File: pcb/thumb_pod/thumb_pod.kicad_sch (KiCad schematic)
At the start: 17 parts, among them J1 Conn_02x06_Odd_Even, SW1 SW_Push, SW2 SW_Push, SW3 SW_Push, SW4 SW_Push, U1 RKJXM1015004

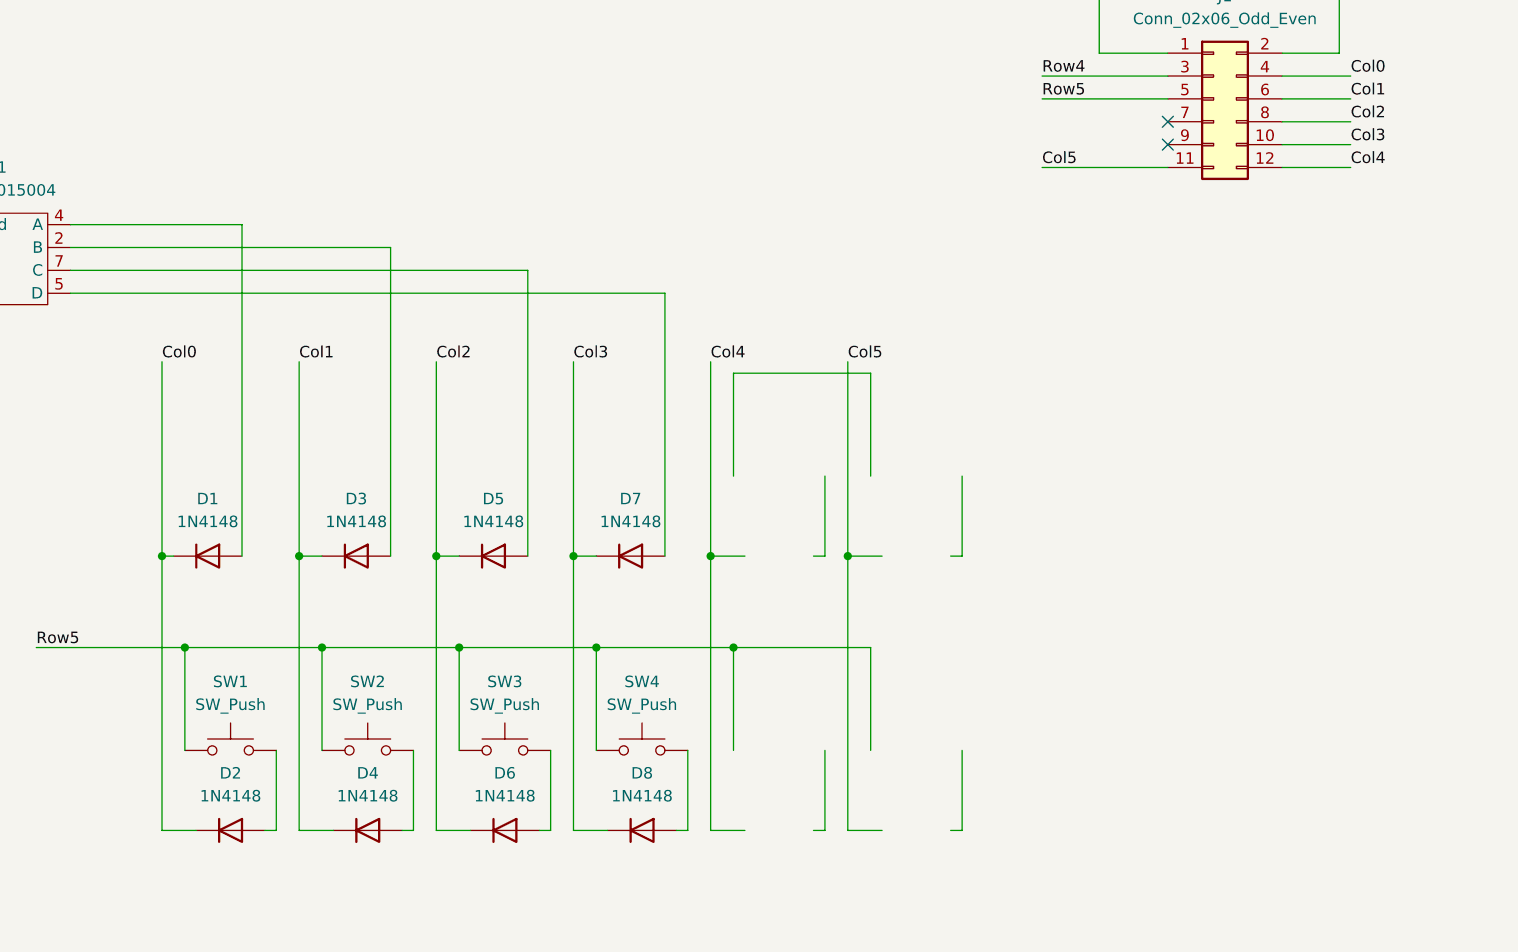
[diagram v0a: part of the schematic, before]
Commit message: - Added multiple positions for each switch to allow for tweaking
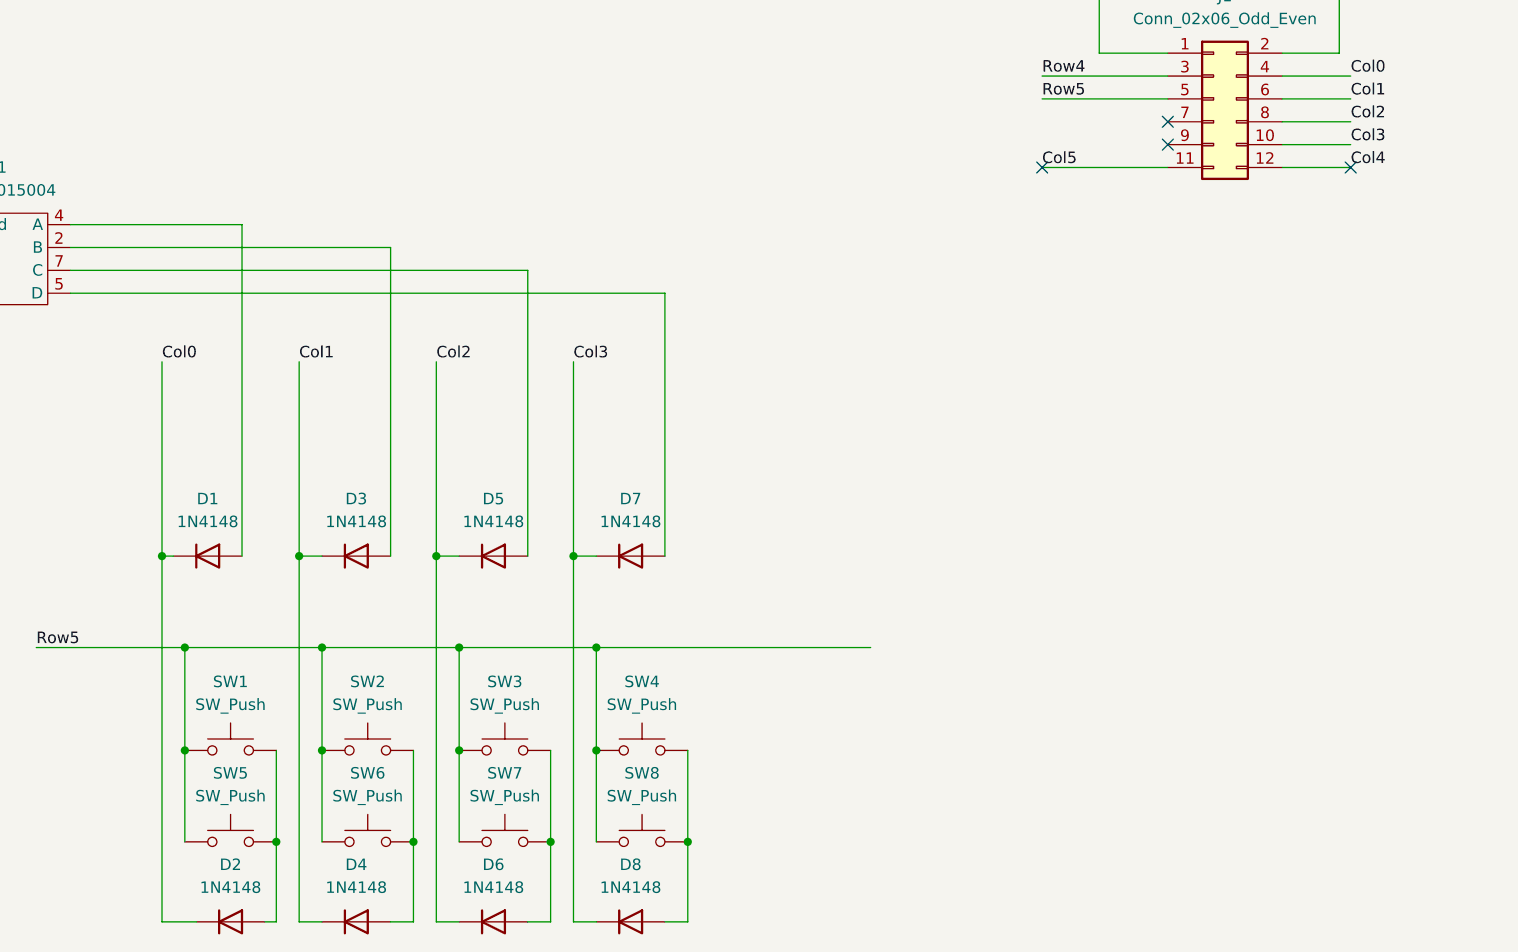
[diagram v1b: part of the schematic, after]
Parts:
- added SW5, SW6, SW7, SW8: SW_Push, keypad:MXOnly-1U-Hotswap, symbol Switch:SW_Push
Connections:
- net Row5: now also SW5.1, SW6.1, SW7.1, SW8.1
- net at D2.2 (A), SW1.2: now also SW5.2
- net at D4.2 (A), SW2.2: now also SW6.2
- net at D8.2 (A), SW4.2: now also SW8.2
- net at D6.2 (A), SW3.2: now also SW7.2
- no-connect marks 4 -> 6
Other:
- moved on the sheet: D2, D4, D6, D8

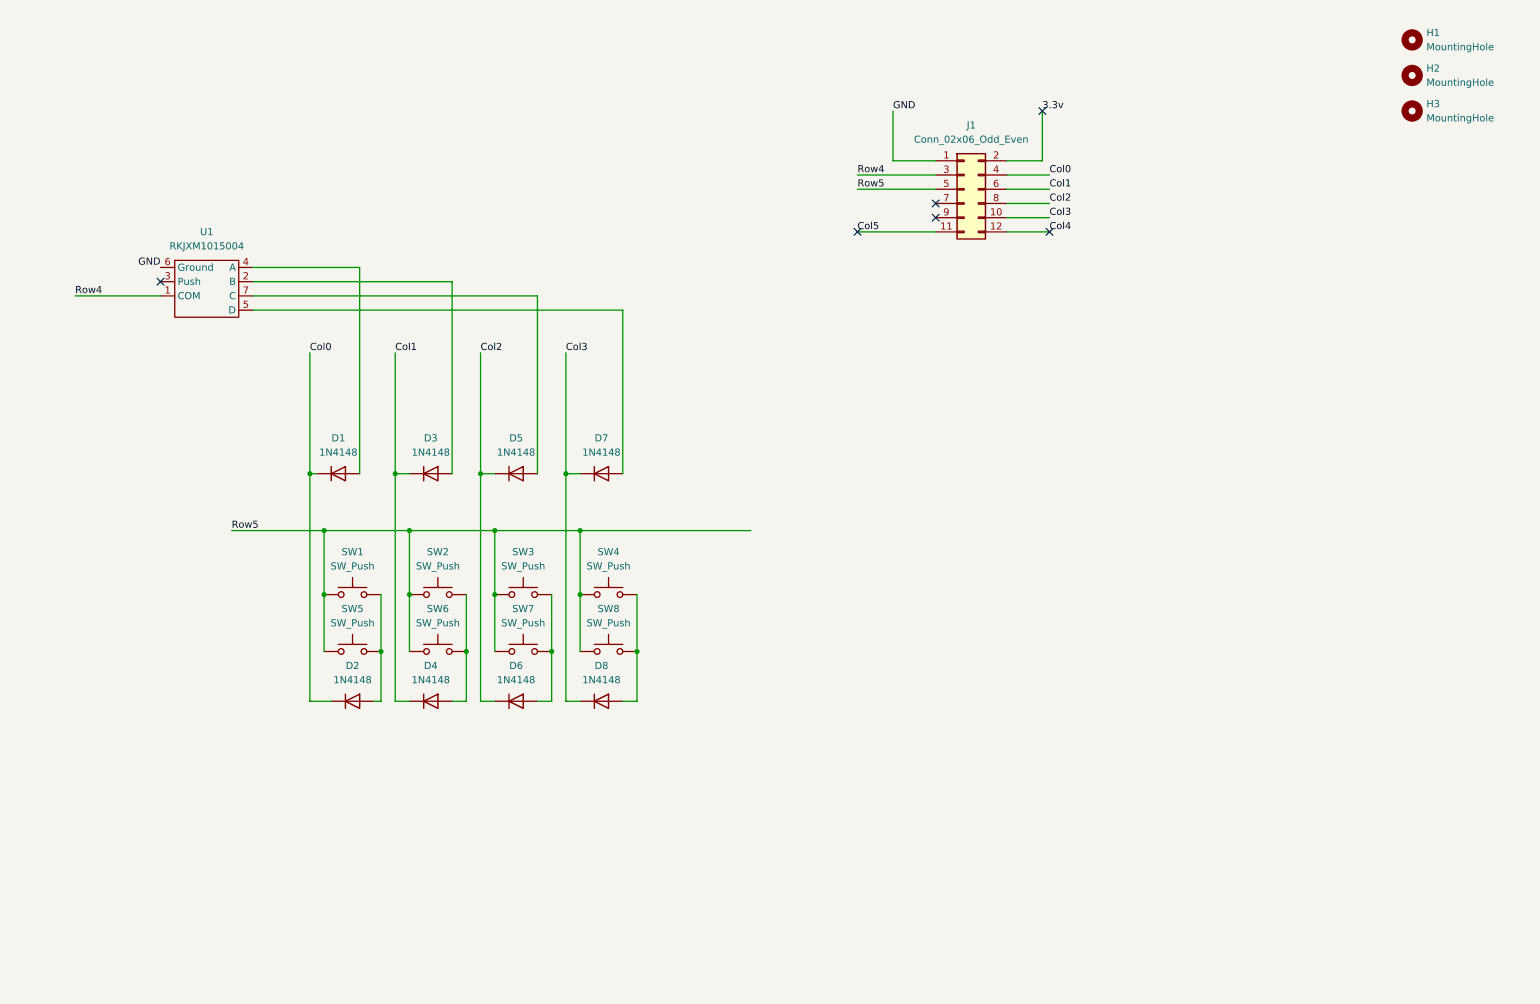
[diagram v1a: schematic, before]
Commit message: - Added a preliminary "mini" thumb pod with only the directional stick  - Added mouse bite footprint from Panelization.pretty
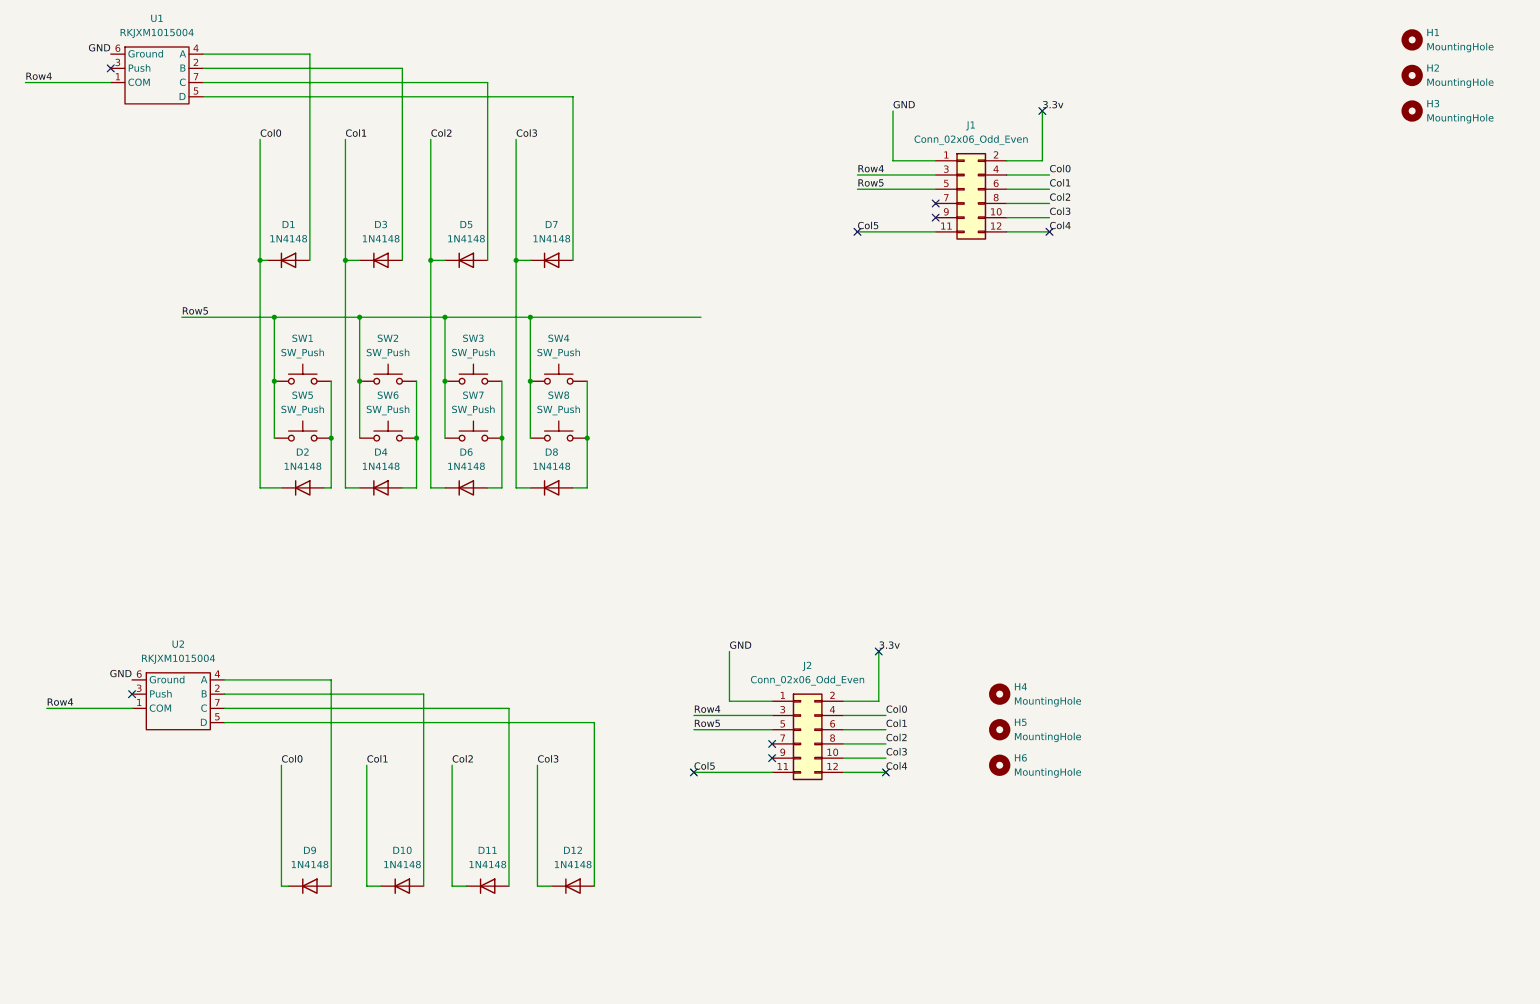
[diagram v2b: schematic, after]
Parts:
- added D10, D11, D12, D9: 1N4148, Diode_THT:D_DO-35_SOD27_P7.62mm_Horizontal, symbol Diode:1N4148
- added H4, H5, H6: MountingHole, MountingHole:MountingHole_3.2mm_M3, symbol Mechanical:MountingHole
- added J2: Conn_02x06_Odd_Even, keypad:PinHeader_2x06_P2.54mm_Horizontal, symbol Connector_Generic:Conn_02x06_Odd_Even
- added U2: RKJXM1015004, thumb_pod:RKJXM1015004, symbol thumb_pod:RKJXM1015004
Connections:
- net 3.3v: now also J2.2 (Pin_2)
- net Col0: now also D9.1 (K), J2.4 (Pin_4)
- net Col1: now also D10.1 (K), J2.6 (Pin_6)
- net Col2: now also D11.1 (K), J2.8 (Pin_8)
- net Col3: now also D12.1 (K), J2.10 (Pin_10)
- net Col4: now also J2.12 (Pin_12)
- net Col5: now also J2.11 (Pin_11)
- net GND: now also J2.1 (Pin_1), U2.6 (Ground)
- net Row4: now also J2.3 (Pin_3), U2.1 (COM)
- net Row5: now also J2.5 (Pin_5)
- new net: D9.2 (A), U2.4 (A)
- new net: D10.2 (A), U2.2 (B)
- new net: D11.2 (A), U2.7 (C)
- new net: D12.2 (A), U2.5 (D)
- no-connect marks 6 -> 12
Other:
- moved on the sheet: D1, D2, D3, D4, D5, D6, D7, D8, SW1, SW2, SW3, SW4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

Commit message: - Added experimental alternate layouts for the thumb pod  - Attempted some DIY panelization
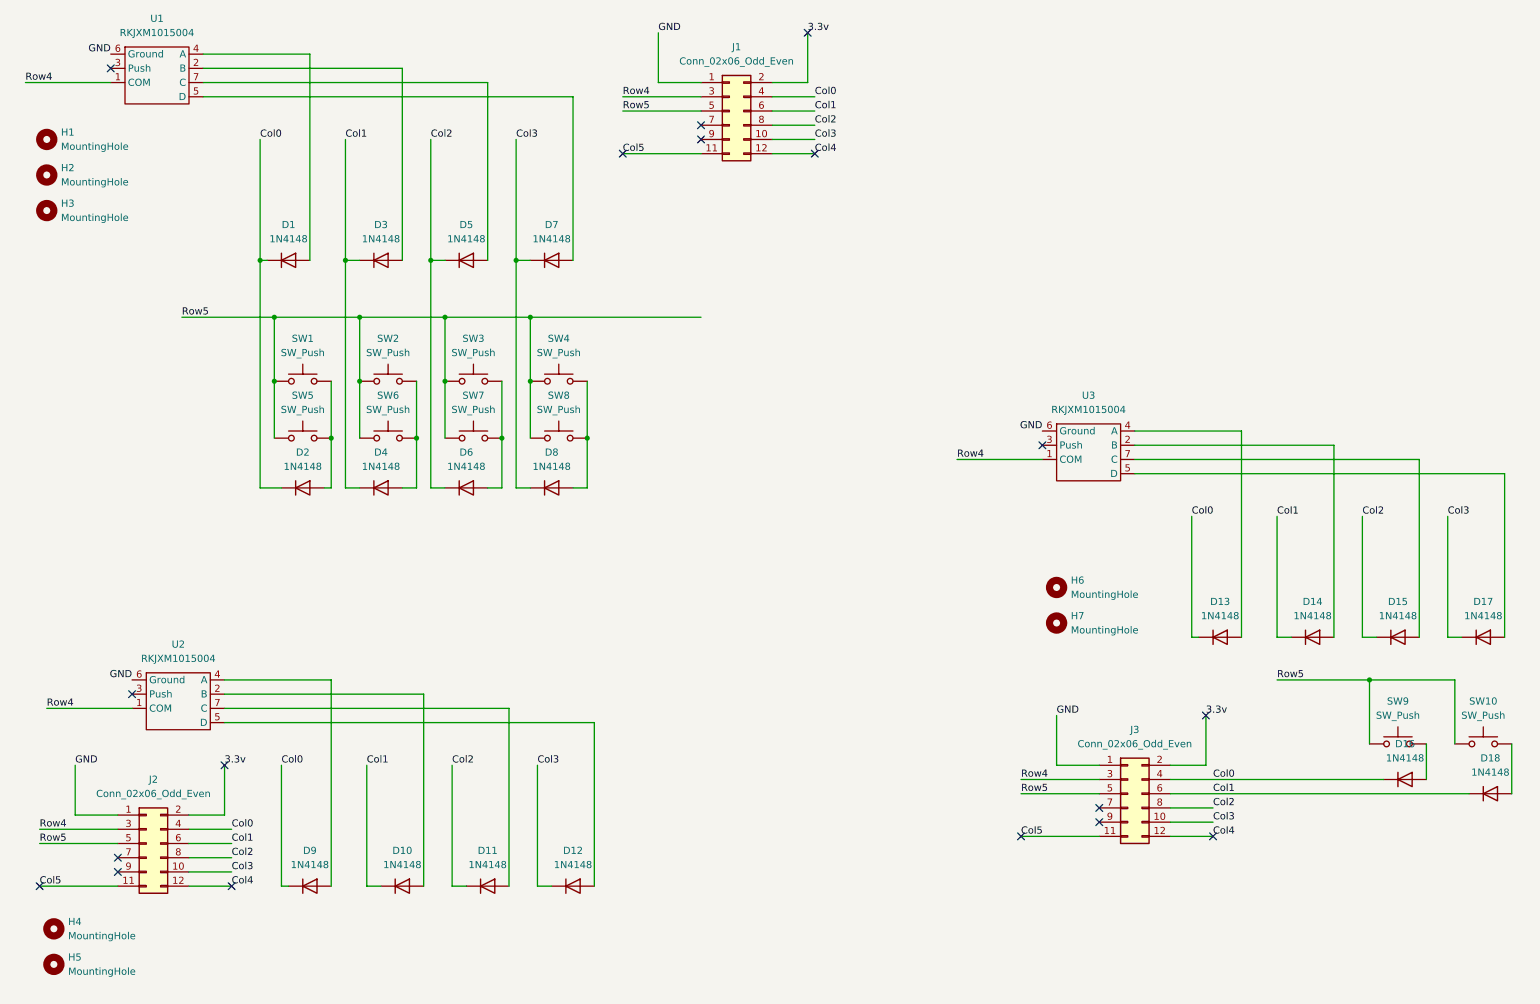
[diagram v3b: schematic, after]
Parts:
- added D13, D14, D15, D16, D17, D18: 1N4148, Diode_THT:D_DO-35_SOD27_P7.62mm_Horizontal, symbol Diode:1N4148
- added H7: MountingHole, MountingHole:MountingHole_3.2mm_M3, symbol Mechanical:MountingHole
- added J3: Conn_02x06_Odd_Even, keypad:PinHeader_2x06_P2.54mm_Horizontal, symbol Connector_Generic:Conn_02x06_Odd_Even
- added SW10, SW9: SW_Push, Button_Switch_THT:SW_PUSH_6mm, symbol Switch:SW_Push
- added U3: RKJXM1015004, thumb_pod:RKJXM1015004, symbol thumb_pod:RKJXM1015004
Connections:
- net 3.3v: now also J3.2 (Pin_2)
- net Col0: now also D13.1 (K), D16.1 (K), J3.4 (Pin_4)
- net Col1: now also D14.1 (K), D18.1 (K), J3.6 (Pin_6)
- net Col2: now also D15.1 (K), J3.8 (Pin_8)
- net Col3: now also D17.1 (K), J3.10 (Pin_10)
- net Col4: now also J3.12 (Pin_12)
- net Col5: now also J3.11 (Pin_11)
- net GND: now also J3.1 (Pin_1), U3.6 (Ground)
- net Row4: now also J3.3 (Pin_3), U3.1 (COM)
- net Row5: now also J3.5 (Pin_5), SW10.1, SW9.1
- new net: D14.2 (A), U3.2 (B)
- new net: D18.2 (A), SW10.2
- new net: D13.2 (A), U3.4 (A)
- new net: D17.2 (A), U3.5 (D)
- new net: D15.2 (A), U3.7 (C)
- new net: D16.2 (A), SW9.2
- no-connect marks 12 -> 18
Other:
- moved on the sheet: H1, H2, H3, H4, H5, J1, J2
